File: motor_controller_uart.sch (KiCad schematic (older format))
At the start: 30 parts, among them J10 DB9_Male, J11 DB9_Male, J8 DB9_Male, J9 DB9_Male, U2 MAX3232, U4 MAX3232

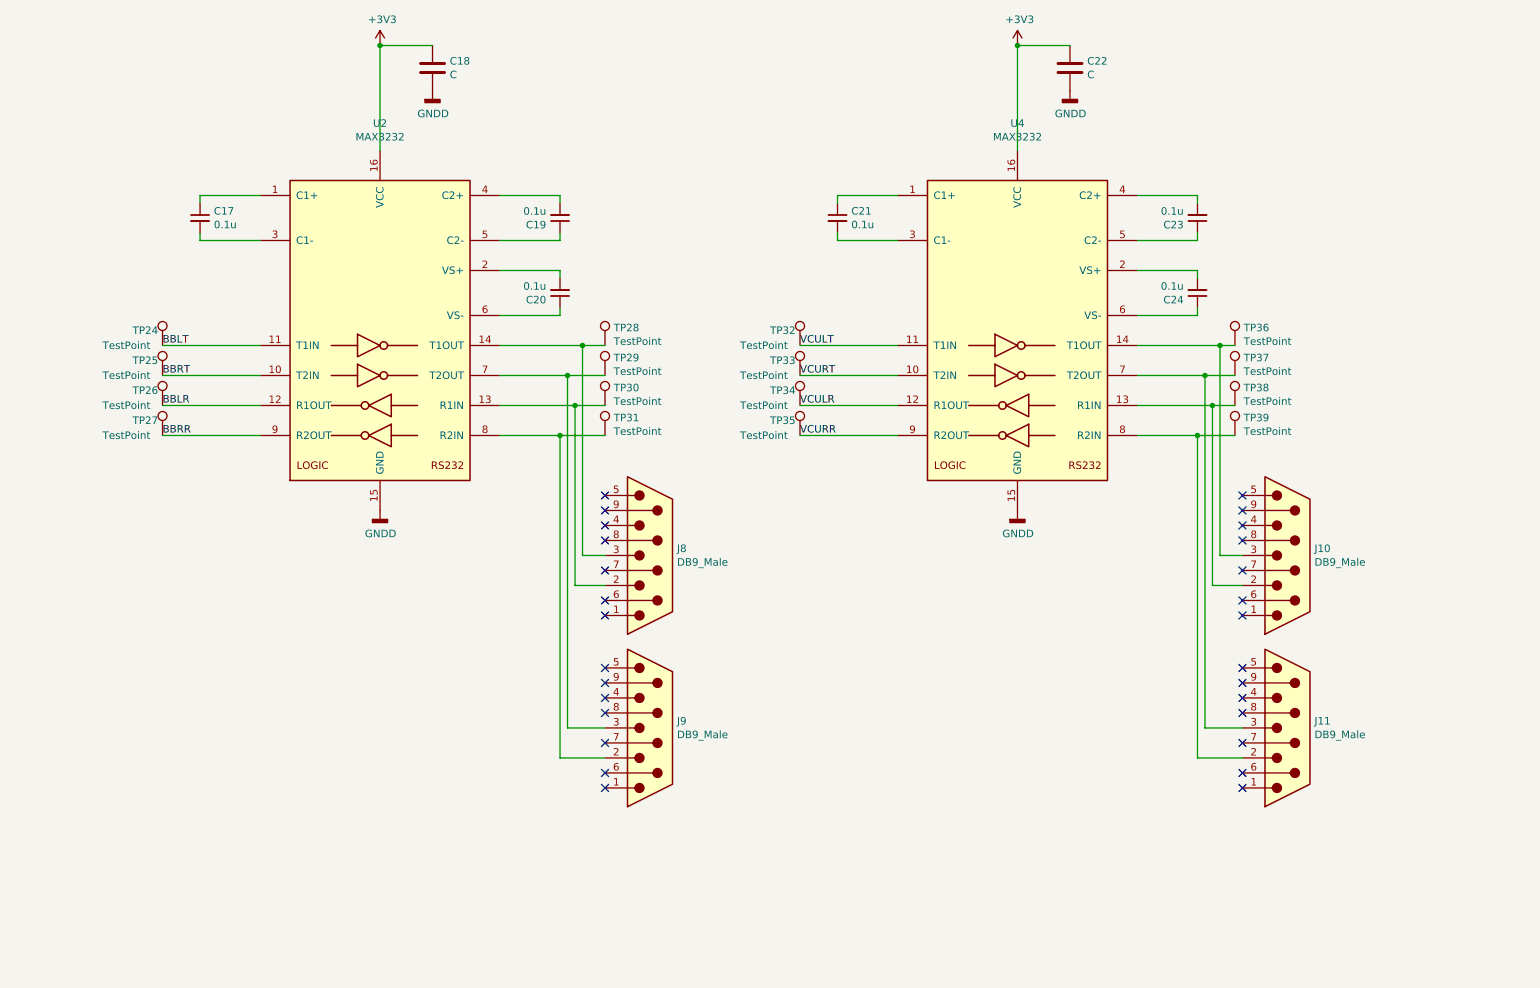
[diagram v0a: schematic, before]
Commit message: removed dac, added jumpers, ready for parting up
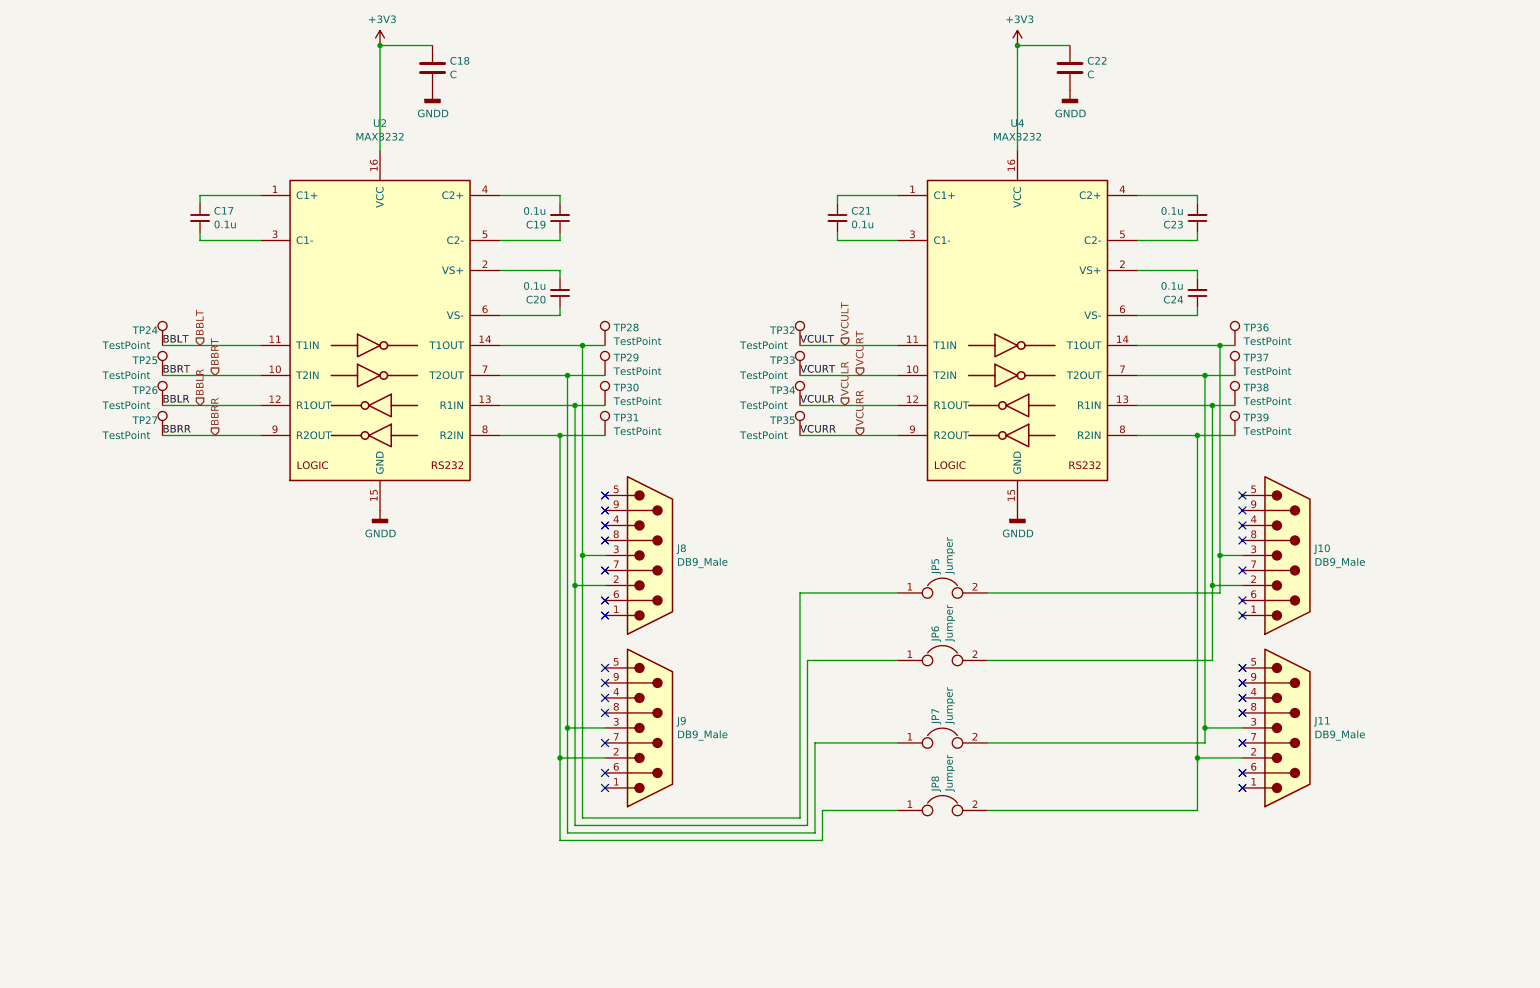
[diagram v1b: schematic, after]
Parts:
- added JP5, JP6, JP7, JP8: Jumper, symbol Device:Jumper
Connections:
- net at J8.2, TP30.1, U2.13 (R1IN): now also JP6.1
- net at J8.3, TP28.1, U2.14 (T1OUT): now also JP5.1
- net at J9.3, TP29.1, U2.7 (T2OUT): now also JP7.1
- net at J9.2, TP31.1, U2.8 (R2IN): now also JP8.1
- net at J10.2, TP38.1, U4.13 (R1IN): now also JP6.2
- net at J10.3, TP36.1, U4.14 (T1OUT): now also JP5.2
- net at J11.3, TP37.1, U4.7 (T2OUT): now also JP7.2
- net at J11.2, TP39.1, U4.8 (R2IN): now also JP8.2
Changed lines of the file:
@@
 	4250 2850 4800 2850
 Wire Wire Line
-	4800 2850 4800 4250
-Wire Wire Line
 	4800 4250 4950 4250
 Wire Wire Line
@@
 Wire Wire Line
 	4650 3450 4650 5600
-Wire Wire Line
-	4650 5600 4950 5600
 NoConn ~ 4950 3850
 NoConn ~ 4950 3950
@@
 	1    0    0    -1
 $EndComp
+Text HLabel 2250 2850 1    50   Input ~ 0
+BBLT
+Text HLabel 2350 3050 1    50   Input ~ 0
+BBRT
+Text HLabel 2250 3250 1    50   Input ~ 0
+BBLR
+Text HLabel 2350 3450 1    50   Input ~ 0
+BBRR
+Text HLabel 6550 2850 1    50   Input ~ 0
+VCULT
+Text HLabel 6650 3050 1    50   Input ~ 0
+VCURT
+Text HLabel 6550 3250 1    50   Input ~ 0
+VCULR
+Text HLabel 6650 3450 1    50   Input ~ 0
+VCURR
+$Comp
+L Device:Jumper JP?
+U 1 1 5E9A899E
+P 7200 4950
+AR Path="/5E9A899E" Ref="JP?"  Part="1"
+AR Path="/5ED986AC/5E9A899E" Ref="JP?"  Part="1"
+AR Path="/5E9860AF/5E9A899E" Ref="JP6"  Part="1"
+F 0 "JP6" V 7154 5077 50  0000 L CNN
+F 1 "Jumper" V 7245 5077 50  0000 L CNN
+F 2 "" H 7200 4950 50  0001 C CNN
+F 3 "~" H 7200 4950 50  0001 C CNN
+	1    7200 4950
+	1    0    0    -1
+$EndComp
+$Comp
+L Device:Jumper JP?
+U 1 1 5E9A89A5
+P 7200 4500
+AR Path="/5E9A89A5" Ref="JP?"  Part="1"
+AR Path="/5ED986AC/5E9A89A5" Ref="JP?"  Part="1"
+AR Path="/5E9860AF/5E9A89A5" Ref="JP5"  Part="1"
+F 0 "JP5" V 7154 4627 50  0000 L CNN
+F 1 "Jumper" V 7245 4627 50  0000 L CNN
+F 2 "" H 7200 4500 50  0001 C CNN
+F 3 "~" H 7200 4500 50  0001 C CNN
+	1    7200 4500
+	1    0    0    -1
+$EndComp
+$Comp
+L Device:Jumper JP?
+U 1 1 5E9BC262
+P 7200 5950
+AR Path="/5E9BC262" Ref="JP?"  Part="1"
+AR Path="/5ED986AC/5E9BC262" Ref="JP?"  Part="1"
+AR Path="/5E9860AF/5E9BC262" Ref="JP8"  Part="1"
+F 0 "JP8" V 7154 6077 50  0000 L CNN
+F 1 "Jumper" V 7245 6077 50  0000 L CNN
+F 2 "" H 7200 5950 50  0001 C CNN
+F 3 "~" H 7200 5950 50  0001 C CNN
+	1    7200 5950
+	1    0    0    -1
+$EndComp
+$Comp
+L Device:Jumper JP?
+U 1 1 5E9BC268
+P 7200 5500
+AR Path="/5E9BC268" Ref="JP?"  Part="1"
+AR Path="/5ED986AC/5E9BC268" Ref="JP?"  Part="1"
+AR Path="/5E9860AF/5E9BC268" Ref="JP7"  Part="1"
+F 0 "JP7" V 7154 5627 50  0000 L CNN
+F 1 "Jumper" V 7245 5627 50  0000 L CNN
+F 2 "" H 7200 5500 50  0001 C CNN
+F 3 "~" H 7200 5500 50  0001 C CNN
+	1    7200 5500
+	1    0    0    -1
+$EndComp
+Connection ~ 4750 4450
+Wire Wire Line
+	7500 4950 9000 4950
+Wire Wire Line
+	9000 4950 9000 4450
+Connection ~ 9000 4450
+Wire Wire Line
+	7500 5500 8950 5500
+Wire Wire Line
+	8950 5500 8950 5400
+Connection ~ 8950 5400
+Wire Wire Line
+	8900 5600 8900 5950
+Wire Wire Line
+	8900 5950 7500 5950
+Connection ~ 8900 5600
+Wire Wire Line
+	9050 4250 9050 4500
+Wire Wire Line
+	7500 4500 9050 4500
+Connection ~ 9050 4250
+Wire Wire Line
+	4650 5600 4950 5600
+Wire Wire Line
+	4800 2850 4800 4250
+Wire Wire Line
+	4800 4250 4800 6000
+Wire Wire Line
+	4800 6000 6250 6000
+Wire Wire Line
+	6250 6000 6250 4500
+Wire Wire Line
+	6250 4500 6900 4500
+Connection ~ 4800 4250
+Wire Wire Line
+	6900 4950 6300 4950
+Wire Wire Line
+	6300 4950 6300 6050
+Wire Wire Line
+	6300 6050 4750 6050
+Wire Wire Line
+	4750 4450 4750 6050
+Wire Wire Line
+	4700 5400 4700 6100
+Wire Wire Line
+	4700 6100 6350 6100
+Wire Wire Line
+	6350 6100 6350 5500
+Wire Wire Line
+	6350 5500 6900 5500
+Connection ~ 4700 5400
+Wire Wire Line
+	6900 5950 6400 5950
+Wire Wire Line
+	6400 5950 6400 6150
+Wire Wire Line
+	6400 6150 4650 6150
+Wire Wire Line
+	4650 6150 4650 5600
+Connection ~ 4650 5600
 $EndSCHEMATC

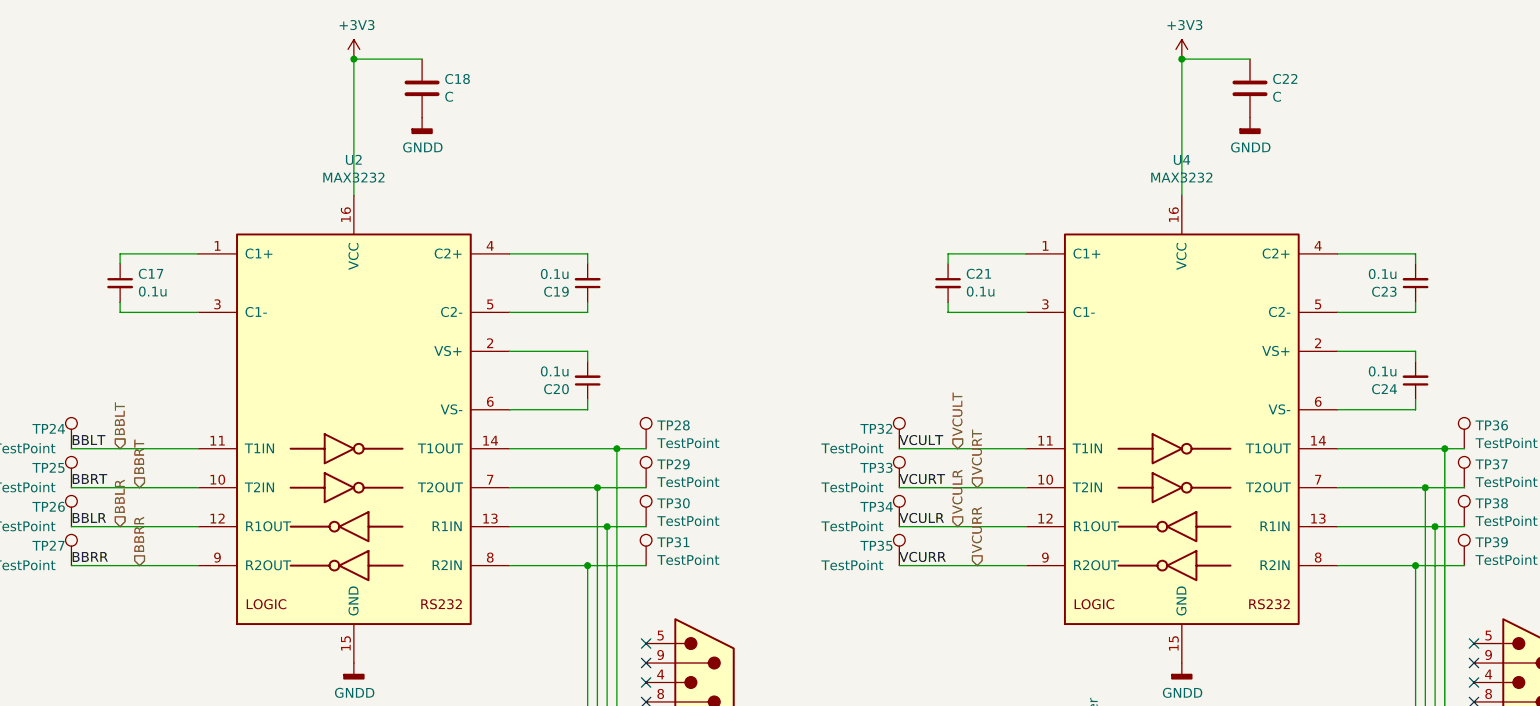
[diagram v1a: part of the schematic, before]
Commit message: parts assigned, layout started, CAN and RS232 sides done
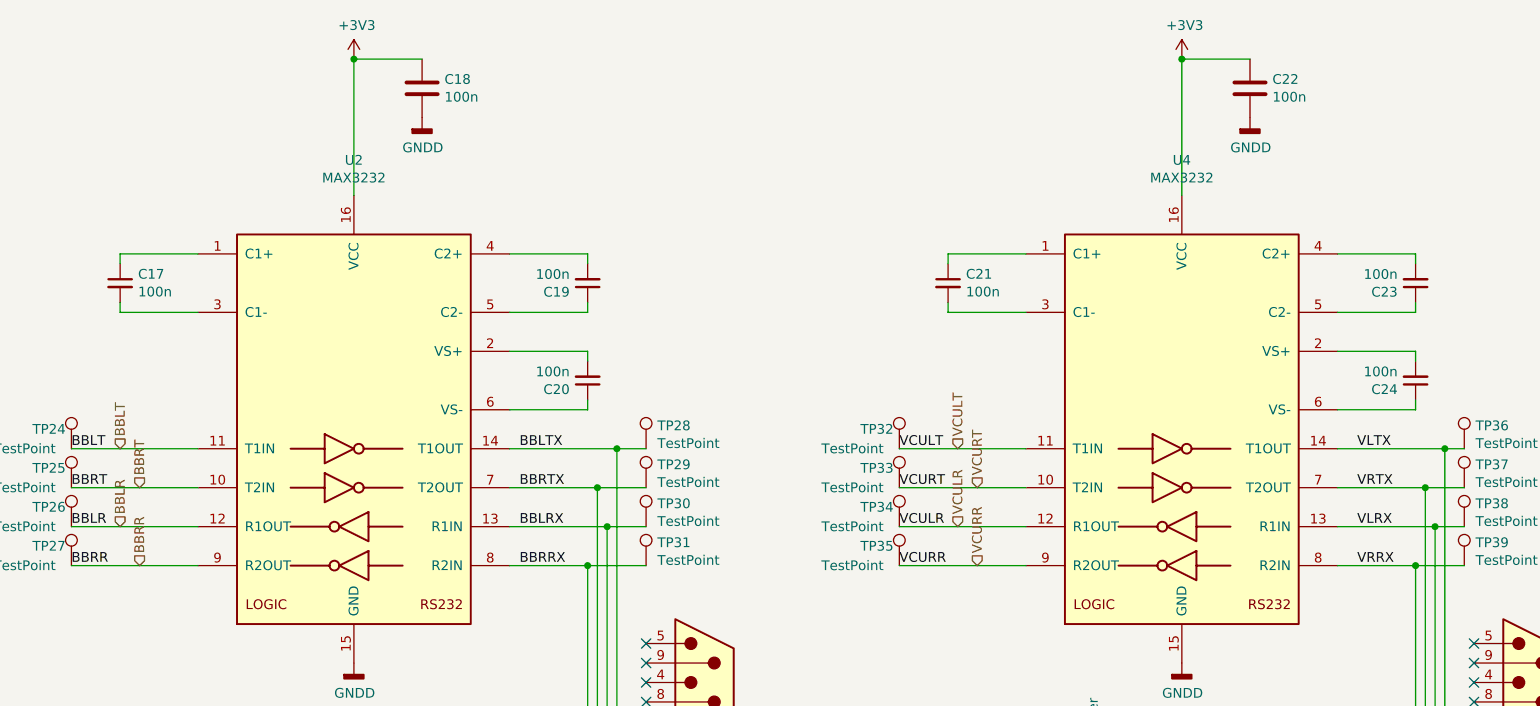
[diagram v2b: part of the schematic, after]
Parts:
- C17, C19, C20, C21, C23, C24: value 0.1u -> 100n; footprint (none) -> Capacitor_SMD:C_0805_2012Metric_Pad1.15x1.40mm_HandSolder
- C18, C22: value C -> 100n; footprint (none) -> Capacitor_SMD:C_0805_2012Metric_Pad1.15x1.40mm_HandSolder
- J10, J11, J8, J9: footprint (none) -> Connector_Dsub:DSUB-9_Male_Horizontal_P2.77x2.84mm_EdgePinOffset7.70mm_Housed_MountingHolesOffset9.12mm; Part (none) -> 5747840-3
- JP5, JP6, JP7, JP8: footprint (none) -> Connector_PinHeader_2.00mm:PinHeader_1x03_P2.00mm_Vertical; Part (none) -> SPN02SXCN-RC; PartB (none) -> M22-2510305
- TP24, TP25, TP26, TP27, TP28, TP29, TP30, TP31, TP32, TP33, TP34, TP35, TP36, TP37, TP38, TP39: footprint (none) -> Connector_PinHeader_2.54mm:PinHeader_1x01_P2.54mm_Vertical
- U2, U4: footprint (none) -> Package_SO:SOIC-16_3.9x9.9mm_P1.27mm; Part (none) -> MAX3232CSE+TCT-ND
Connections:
- net BBLRX: now reaches J8.2, JP6.1, TP30.1, U2.13 (R1IN)
- net VLRX: now reaches J10.2, JP6.2, TP38.1, U4.13 (R1IN)
- net BBLTX: now reaches J8.3, JP5.1, TP28.1, U2.14 (T1OUT)
- net VLTX: now reaches J10.3, JP5.2, TP36.1, U4.14 (T1OUT)
- net BBRRX: now reaches J9.2, JP8.1, TP31.1, U2.8 (R2IN)
- net VRRX: now reaches J11.2, JP8.2, TP39.1, U4.8 (R2IN)
- net BBRTX: now reaches J9.3, JP7.1, TP29.1, U2.7 (T2OUT)
- net VRTX: now reaches J11.3, JP7.2, TP37.1, U4.7 (T2OUT)

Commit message: new, compact (and sexy) design
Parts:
- removed JP5, JP6, JP7: Jumper, Connector_PinHeader_2.00mm:PinHeader_1x03_P2.00mm_Vertical, symbol Device:Jumper
- added JP10, JP11, JP12: Jumper, Connector_PinHeader_2.00mm:PinHeader_1x03_P2.00mm_Vertical, symbol Device:Jumper
- added JP13, JP14, JP15, JP16, JP5, JP6, JP7, JP9: Jumper_3_Bridged12, Connector_PinHeader_2.00mm:PinHeader_1x03_P2.00mm_Vertical, symbol Jumper:Jumper_3_Bridged12
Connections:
- net BBLRX: now also JP9.2 (C); no longer J8.2
- net BBLTX: now also JP7.2 (C); no longer J8.3
- net BBRRX: now also JP6.2 (C); no longer J9.2, JP8.1
- net BBRTX: now also JP5.2 (C); no longer J9.3
- net VLRX: now also JP16.2 (C); no longer J10.2
- net VLTX: now also JP15.2 (C); no longer J10.3
- net VRRX: now also JP14.2 (C); no longer J11.2, JP8.2
- net VRTX: now also JP13.2 (C); no longer J11.3
- new net: J9.3, JP12.1, JP7.1 (A), JP9.3 (B)
- new net: J9.2, JP7.3 (B), JP8.1, JP9.1 (A)
- new net: J8.3, JP10.1, JP5.1 (A), JP6.3 (B)
- new net: J8.2, JP11.1, JP5.3 (B), JP6.1 (A)
- new net: J11.3, JP12.2, JP15.1 (A), JP16.3 (B)
- new net: J11.2, JP15.3 (B), JP16.1 (A), JP8.2
- new net: J10.3, JP10.2, JP13.1 (A), JP14.3 (B)
- new net: J10.2, JP11.2, JP13.3 (B), JP14.1 (A)
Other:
- note added: "L"
- note added: "R"
- moved on the sheet: J10, J11, J8, J9, JP8

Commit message: forgot to save schematic
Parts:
- J10, J11, J8, J9: footprint Connector_Dsub:DSUB-9_Male_Horizontal_P2.77x2.84mm_EdgePinOffset7.70mm_Housed_MountingHolesOffset9.12mm -> Connector_Dsub:DSUB-9_Male_Vertical_P2.77x2.84mm_MountingHoles
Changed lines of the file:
@@
 F 0 "J8" H 1780 5196 50  0000 L CNN
 F 1 "DB9_Male" H 1780 5105 50  0000 L CNN
-F 2 "Connector_Dsub:DSUB-9_Male_Horizontal_P2.77x2.84mm_EdgePinOffset7.70mm_Housed_MountingHolesOffset9.12mm" H 1600 5150 50  0001 C CNN
+F 2 "Connector_Dsub:DSUB-9_Male_Vertical_P2.77x2.84mm_MountingHoles" H 1600 5150 50  0001 C CNN
 F 3 " ~" H 1600 5150 50  0001 C CNN
 F 4 "5747840-3" H 1600 5150 50  0001 C CNN "Part"
@@
 F 0 "J9" H 1780 6346 50  0000 L CNN
 F 1 "DB9_Male" H 1780 6255 50  0000 L CNN
-F 2 "Connector_Dsub:DSUB-9_Male_Horizontal_P2.77x2.84mm_EdgePinOffset7.70mm_Housed_MountingHolesOffset9.12mm" H 1600 6300 50  0001 C CNN
+F 2 "Connector_Dsub:DSUB-9_Male_Vertical_P2.77x2.84mm_MountingHoles" H 1600 6300 50  0001 C CNN
 F 3 " ~" H 1600 6300 50  0001 C CNN
 F 4 "5747840-3" H 1600 6300 50  0001 C CNN "Part"
@@
 F 0 "J10" H 10680 4846 50  0000 L CNN
 F 1 "DB9_Male" H 10680 4755 50  0000 L CNN
-F 2 "Connector_Dsub:DSUB-9_Male_Horizontal_P2.77x2.84mm_EdgePinOffset7.70mm_Housed_MountingHolesOffset9.12mm" H 10500 4800 50  0001 C CNN
+F 2 "Connector_Dsub:DSUB-9_Male_Vertical_P2.77x2.84mm_MountingHoles" H 10500 4800 50  0001 C CNN
 F 3 " ~" H 10500 4800 50  0001 C CNN
 F 4 "5747840-3" H 10500 4800 50  0001 C CNN "Part"
@@
 F 0 "J11" H 10680 5996 50  0000 L CNN
 F 1 "DB9_Male" H 10680 5905 50  0000 L CNN
-F 2 "Connector_Dsub:DSUB-9_Male_Horizontal_P2.77x2.84mm_EdgePinOffset7.70mm_Housed_MountingHolesOffset9.12mm" H 10500 5950 50  0001 C CNN
+F 2 "Connector_Dsub:DSUB-9_Male_Vertical_P2.77x2.84mm_MountingHoles" H 10500 5950 50  0001 C CNN
 F 3 " ~" H 10500 5950 50  0001 C CNN
 F 4 "5747840-3" H 10500 5950 50  0001 C CNN "Part"

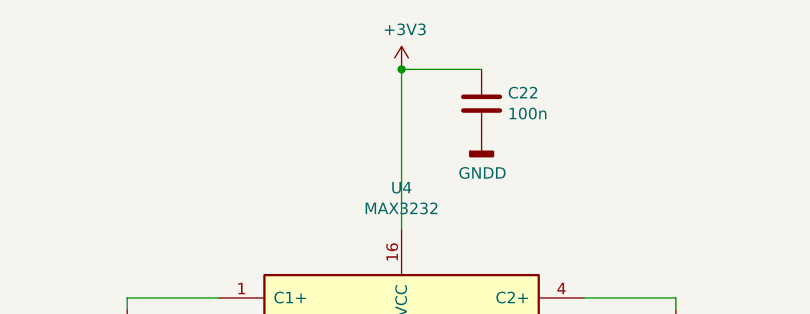
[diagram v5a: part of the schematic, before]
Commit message: better routing, tcan footprint, mount holes + silkscreen
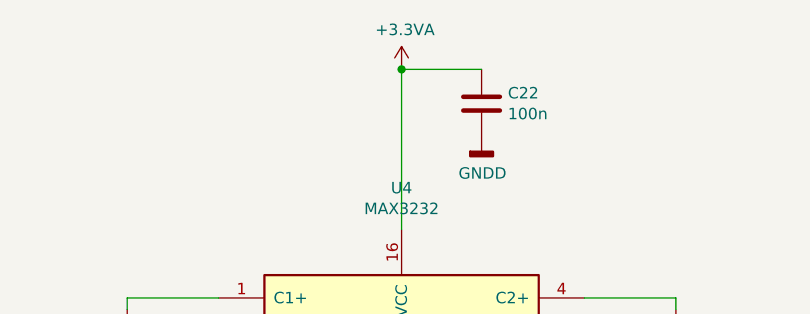
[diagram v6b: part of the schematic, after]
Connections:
- net +3V3: no longer C22.1, U4.16 (VCC)
- new net +3.3VA: C22.1, U4.16 (VCC)
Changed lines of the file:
@@
 	7700 1550 7700 850
-$Comp
-L power:+3V3 #PWR0126
-U 1 1 5EB3D913
-P 7700 850
-F 0 "#PWR0126" H 7700 700 50  0001 C CNN
-F 1 "+3V3" H 7715 1023 50  0000 C CNN
-F 2 "" H 7700 850 50  0001 C CNN
-F 3 "" H 7700 850 50  0001 C CNN
-	1    7700 850
-	1    0    0    -1
-$EndComp
-Connection ~ 7700 850
 $Comp
 L power:GNDD #PWR0127
@@
 Text Label 8100 4550 0    50   ~ 0
 VRRX
+$Comp
+L power:+3.3VA #PWR?
+U 1 1 5F36242E
+P 7700 850
+AR Path="/5F36242E" Ref="#PWR?"  Part="1"
+AR Path="/5E9860AF/5F36242E" Ref="#PWR0119"  Part="1"
+F 0 "#PWR0119" H 7700 700 50  0001 C CNN
+F 1 "+3.3VA" H 7715 1023 50  0000 C CNN
+F 2 "" H 7700 850 50  0001 C CNN
+F 3 "" H 7700 850 50  0001 C CNN
+	1    7700 850
+	1    0    0    -1
+$EndComp
+Connection ~ 7700 850
 $EndSCHEMATC
